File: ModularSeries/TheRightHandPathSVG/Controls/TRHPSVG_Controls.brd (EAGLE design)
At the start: 200 x 100 mm, 76 parts, among them SW1 SPDT_SWITCHDW1, SW10 SPDT_SWITCHDW1, SW11 SPDT_SWITCHDW1, SW12 SPDT_SWITCHDW1, SW13 SPDT_SWITCHDW1, SW14 SPDT_SWITCHDW1, SW15 SPDT_SWITCHDW1, SW16 SPDT_SWITCHDW1, SW17 SPDT_SWITCHDW1, SW2 SPDT_SWITCHDW1, SW3 SPDT_SWITCHDW1, SW4 SPDT_SWITCHDW1, SW5 SPDT_SWITCHDW1, SW6 SPDT_SWITCHDW1, SW7 SPDT_SWITCHDW1, SW8 SPDT_SWITCHDW1, SW9 SPDT_SWITCHDW1

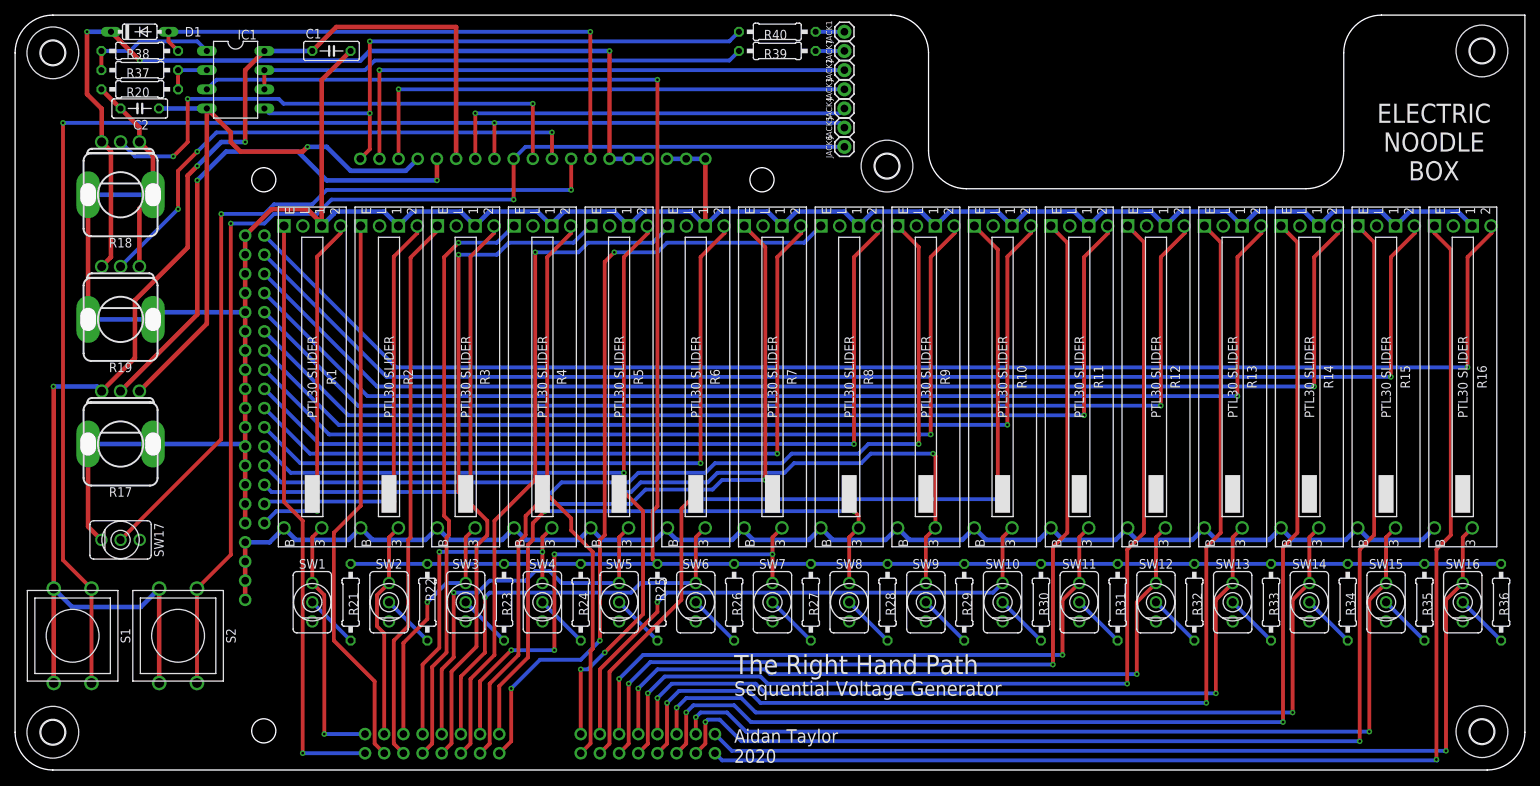
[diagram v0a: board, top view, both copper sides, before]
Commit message: Updates to ARFG schematic - not included in layout yet
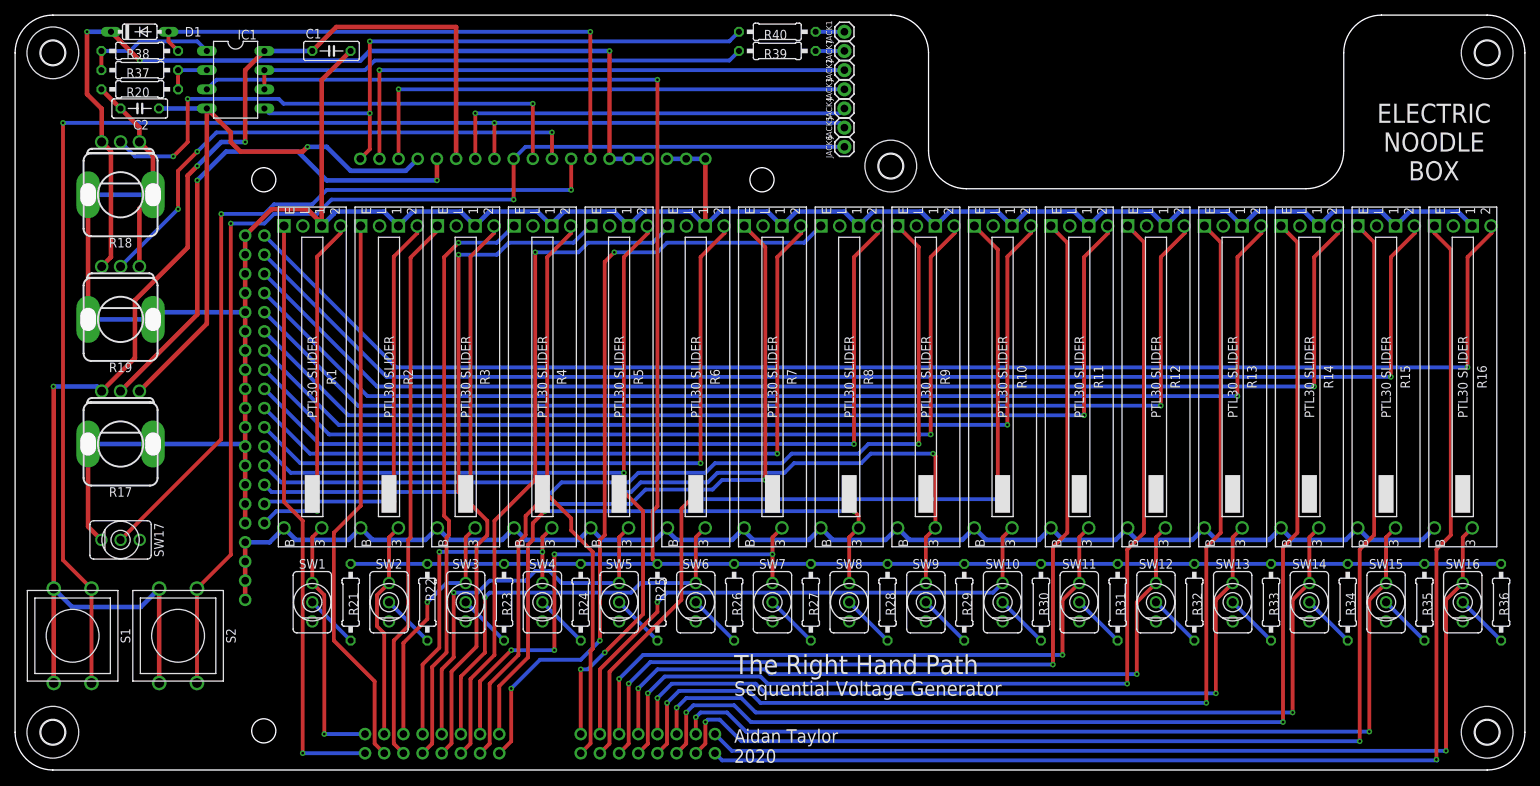
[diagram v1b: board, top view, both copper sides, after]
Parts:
- moved H4 0.73 mm to (195.0, 95.0)
- moved H2 0.69 mm to (195.0, 5.00)
- moved H5 0.50 mm to (116.0, 80.0)
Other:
- outline, holes or cut-outs redrawn
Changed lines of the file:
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@@
 <setting verticaltext="up"/>
 </settings>
-<grid distance="25" unitdist="mil" unit="mil" style="lines" multiple="1" display="no" altdistance="5" altunitdist="mil" altunit="mil"/>
+<grid distance="25" unitdist="mil" unit="mm" style="lines" multiple="1" display="no" altdistance="5" altunitdist="mil" altunit="mil"/>
 <layers>
 <layer number="1" name="Top" color="4" fill="1" visible="yes" active="yes"/>
@@
 <wire x1="5" y1="0" x2="195" y2="0" width="0" layer="20"/>
 <wire x1="195" y1="0" x2="200" y2="5" width="0" layer="20" curve="90"/>
-<wire x1="200" y1="5" x2="200" y2="100" width="0" layer="20"/>
+<wire x1="181" y1="100" x2="195" y2="100" width="0" layer="20"/>
+<wire x1="195" y1="100" x2="200" y2="95" width="0" layer="20" curve="-90"/>
+<wire x1="200" y1="95" x2="200" y2="5" width="0" layer="20"/>
 <wire x1="176" y1="82" x2="176" y2="95" width="0" layer="20"/>
 <wire x1="176" y1="95" x2="181" y2="100" width="0" layer="20" curve="-90"/>
-<wire x1="181" y1="100" x2="200" y2="100" width="0" layer="20"/>
 <wire x1="5" y1="100" x2="116" y2="100" width="0" layer="20"/>
 <wire x1="116" y1="100" x2="121" y2="95" width="0" layer="20" curve="-90"/>
@@
 <attribute name="POPULARITY" value="7" x="5" y="5" size="1.778" layer="27" display="off"/>
 </element>
-<element name="H2" library="holes" library_urn="urn:adsk.eagle:library:237" package="3,2" package3d_urn="urn:adsk.eagle:package:14275/1" value="MOUNT-HOLE3.2" x="194.31" y="5.08" smashed="yes">
-<attribute name="POPULARITY" value="7" x="194.31" y="5.08" size="1.778" layer="27" display="off"/>
+<element name="H2" library="holes" library_urn="urn:adsk.eagle:library:237" package="3,2" package3d_urn="urn:adsk.eagle:package:14275/1" value="MOUNT-HOLE3.2" x="195" y="5" smashed="yes">
+<attribute name="POPULARITY" value="7" x="195" y="5" size="1.778" layer="27" display="off"/>
 </element>
 <element name="H3" library="holes" library_urn="urn:adsk.eagle:library:237" package="3,2" package3d_urn="urn:adsk.eagle:package:14275/1" value="MOUNT-HOLE3.2" x="5" y="95" smashed="yes">
 <attribute name="POPULARITY" value="7" x="5" y="95" size="1.778" layer="27" display="off"/>
 </element>
-<element name="H4" library="holes" library_urn="urn:adsk.eagle:library:237" package="3,2" package3d_urn="urn:adsk.eagle:package:14275/1" value="MOUNT-HOLE3.2" x="194.31" y="95.25" smashed="yes">
-<attribute name="POPULARITY" value="7" x="194.31" y="95.25" size="1.778" layer="27" display="off"/>
+<element name="H4" library="holes" library_urn="urn:adsk.eagle:library:237" package="3,2" package3d_urn="urn:adsk.eagle:package:14275/1" value="MOUNT-HOLE3.2" x="195" y="95" smashed="yes">
+<attribute name="POPULARITY" value="7" x="195" y="95" size="1.778" layer="27" display="off"/>
 </element>
 <element name="SW17" library="ElectricNoodleBox" package="MICRODPDT-DW1" value="SPDT_SWITCHDW1" x="13.97" y="30.48" smashed="yes" rot="R90">
 <attribute name="NAME" x="19.05" y="30.48" size="1.27" layer="25" rot="R90" align="center"/>
 </element>
-<element name="H5" library="holes" library_urn="urn:adsk.eagle:library:237" package="3,2" package3d_urn="urn:adsk.eagle:package:14275/1" value="MOUNT-HOLE3.2" x="115.5" y="80" smashed="yes">
-<attribute name="POPULARITY" value="7" x="115.5" y="80" size="1.778" layer="27" display="off"/>
+<element name="H5" library="holes" library_urn="urn:adsk.eagle:library:237" package="3,2" package3d_urn="urn:adsk.eagle:package:14275/1" value="MOUNT-HOLE3.2" x="116" y="80" smashed="yes">
+<attribute name="POPULARITY" value="7" x="116" y="80" size="1.778" layer="27" display="off"/>
 </element>
 </elements>
